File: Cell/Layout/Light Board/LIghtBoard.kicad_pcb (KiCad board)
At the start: 2 copper layers, 59.8 x 30.5 mm, 12 parts, among them J1 Conn_01x03, J2 Conn_01x03

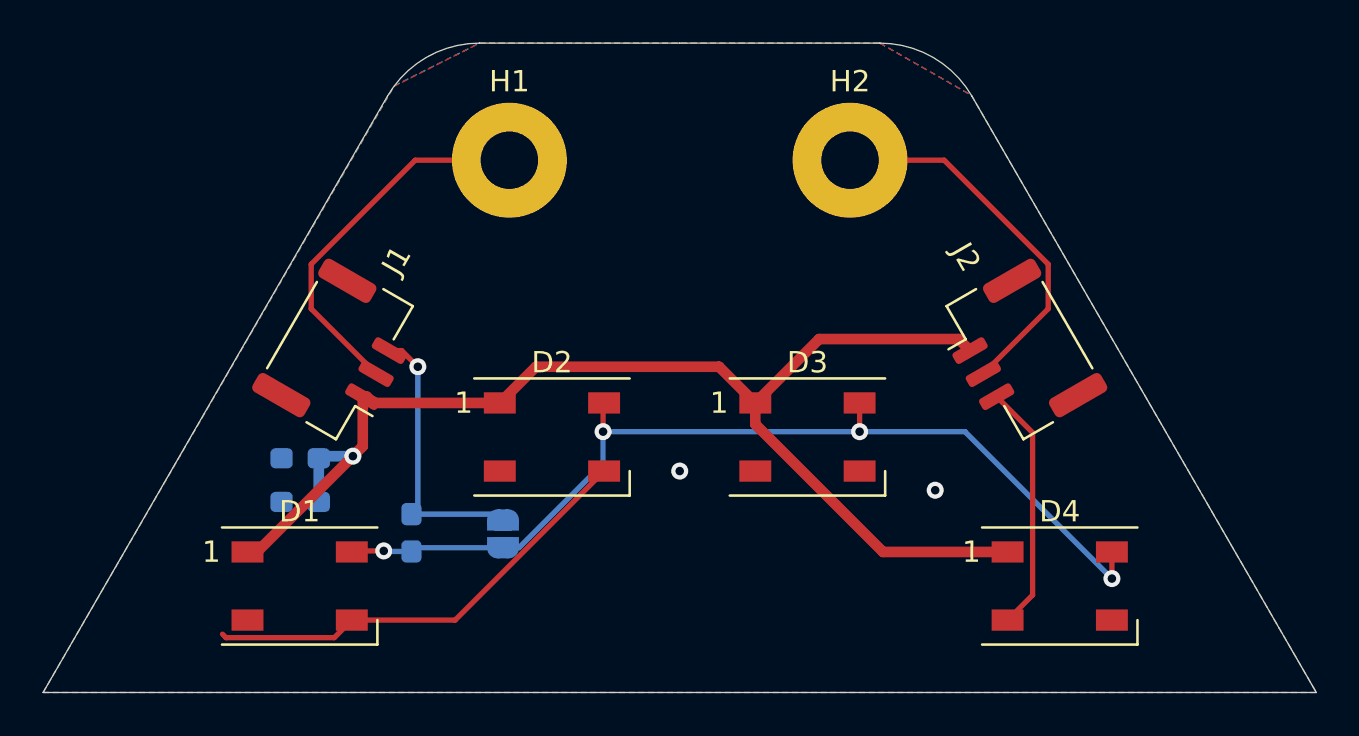
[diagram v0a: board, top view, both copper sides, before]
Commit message: Finish layouts
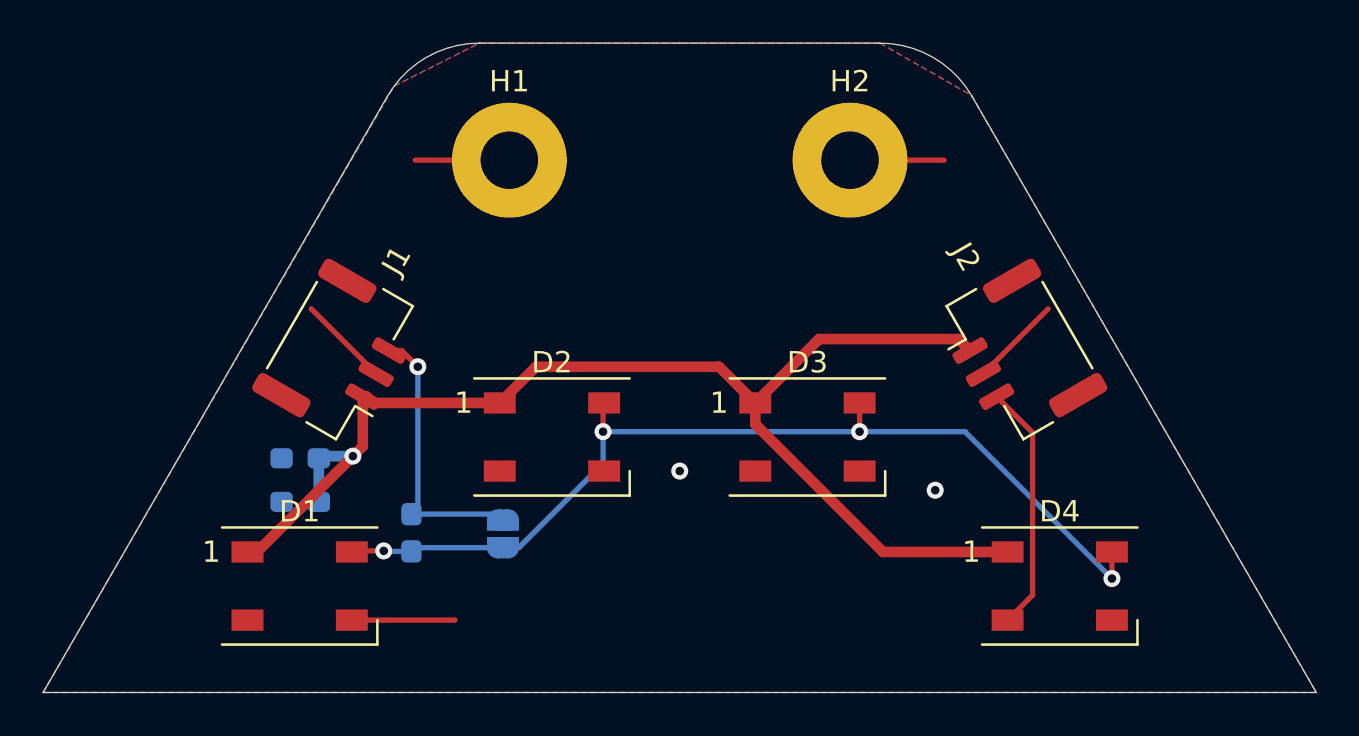
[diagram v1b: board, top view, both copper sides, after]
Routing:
- net GND: track 57.2 -> 22.8 mm
